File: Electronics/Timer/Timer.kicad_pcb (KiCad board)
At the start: 2 copper layers, 13 parts, among them J1 RJ12-UNSHLD, U1 74HC165

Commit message: Updated trace routing on timer circuit
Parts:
- moved C1 29.8 mm to (75.5, 66.0)
- moved C2 29.8 mm to (44.2, 41.2)
- moved D1 29.8 mm to (64.2, 41.2)
- moved D2 29.8 mm to (71.5, 51.0)
- moved J1 29.8 mm to (61.2, 21.2)
- moved R1 29.8 mm to (74.5, 47.2)
- moved RN1 29.8 mm to (53.8, 65.8)
- moved S1 29.8 mm to (33.0, 82.0)
- moved S2 29.8 mm to (46.5, 80.2)
- moved S3 29.8 mm to (59.2, 80.5)
- moved S4 29.8 mm to (71.2, 80.5)
- moved S5 29.8 mm to (96.5, 81.5)
- moved U1 29.8 mm to (69.0, 54.0)
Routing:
- net Net-(RN1-Pad6): track 34.0 -> 79.9 mm, vias 0 -> 2
- net /LOAD: track 0.00 -> 36.2 mm, vias 0 -> 2
- net GND: track 182.5 -> 186.4 mm
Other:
- board outline added: 86.2 x 73.5 mm

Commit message: Updated Timer schematic and updated PCB footprints
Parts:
- added C3: 270pF, Capacitors_SMD:C_0603_HandSoldering, B.Cu at (49.8, 44.2)
- added D3: D_Zener, Diodes_SMD:SOD-80C, B.Cu at (49.5, 48.3)
- added D4: D_Zener, Diodes_SMD:SOD-80C, B.Cu at (70.9, 29.2)
- added R2: 10, Resistors_SMD:R_1206_HandSoldering, B.Cu at (59.2, 44.7)
- added R3: 470, Resistors_SMD:R_1206_HandSoldering, B.Cu at (43.9, 46.2)
- added R4: 470, Resistors_SMD:R_1206_HandSoldering, B.Cu at (59.4, 32.8)
- C1: value C -> 270pF; footprint Capacitors_THT:C_Disc_D4.3mm_W1.9mm_P5.00mm -> Capacitors_SMD:C_0603_HandSoldering; moved to B.Cu
- C2: value CP1 -> 10uF; footprint Capacitors_THT:CP_Axial_L10.0mm_D6.0mm_P15.00mm_Horizontal -> Capacitors_SMD:C_1210_HandSoldering; moved to B.Cu
- D2: value D -> D_Zener; footprint Diodes_THT:D_A-405_P5.08mm_Vertical_AnodeUp -> Diodes_SMD:SOD-80C; moved to B.Cu
- R1: value R -> 68; footprint Resistors_THT:R_Axial_DIN0309_L9.0mm_D3.2mm_P2.54mm_Vertical -> Resistors_SMD:R_1206_HandSoldering; moved to B.Cu
- moved C1 19.3 mm to (62.5, 51.8)
- moved C2 14.0 mm to (56.4, 48.3), turned to 180 degrees
- moved D2 8.22 mm to (63.8, 48.3)
- moved R1 7.47 mm to (67.3, 45.2), turned to 0 degrees
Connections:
- D2 pad 2: /CLK -> GND
- J1 pad 2: /CLK -> Net-(J1-Pad2)
- J1 pad 3: /LOAD -> Net-(J1-Pad3)
- J1 pad 4: Net-(J1-Pad4) -> Net-(C3-Pad1)
- R1 pad 1: +3V3 -> Net-(J1-Pad2)
- U1 pad 2: /CLK -> +3V3
- U1 pad 9: Net-(J1-Pad4) -> Net-(D3-Pad1)
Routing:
- net Net-(J1-Pad4): track 70.6 -> 0.00 mm
- net Net-(C3-Pad1): track 0.00 -> 62.6 mm
- net GND: track 186.4 -> 234.8 mm
- net /CLK: track 28.3 -> 0.00 mm
- net Net-(J1-Pad2): track 0.00 -> 25.2 mm
- net Net-(D3-Pad1): track 0.00 -> 20.4 mm
- net +3V3: track 223.2 -> 203.0 mm
- net Net-(J1-Pad3): track 0.00 -> 7.80 mm
- net /LOAD: track 36.2 -> 40.1 mm, vias 2 -> 0
- net Net-(D1-Pad2): track 3.50 -> 6.74 mm

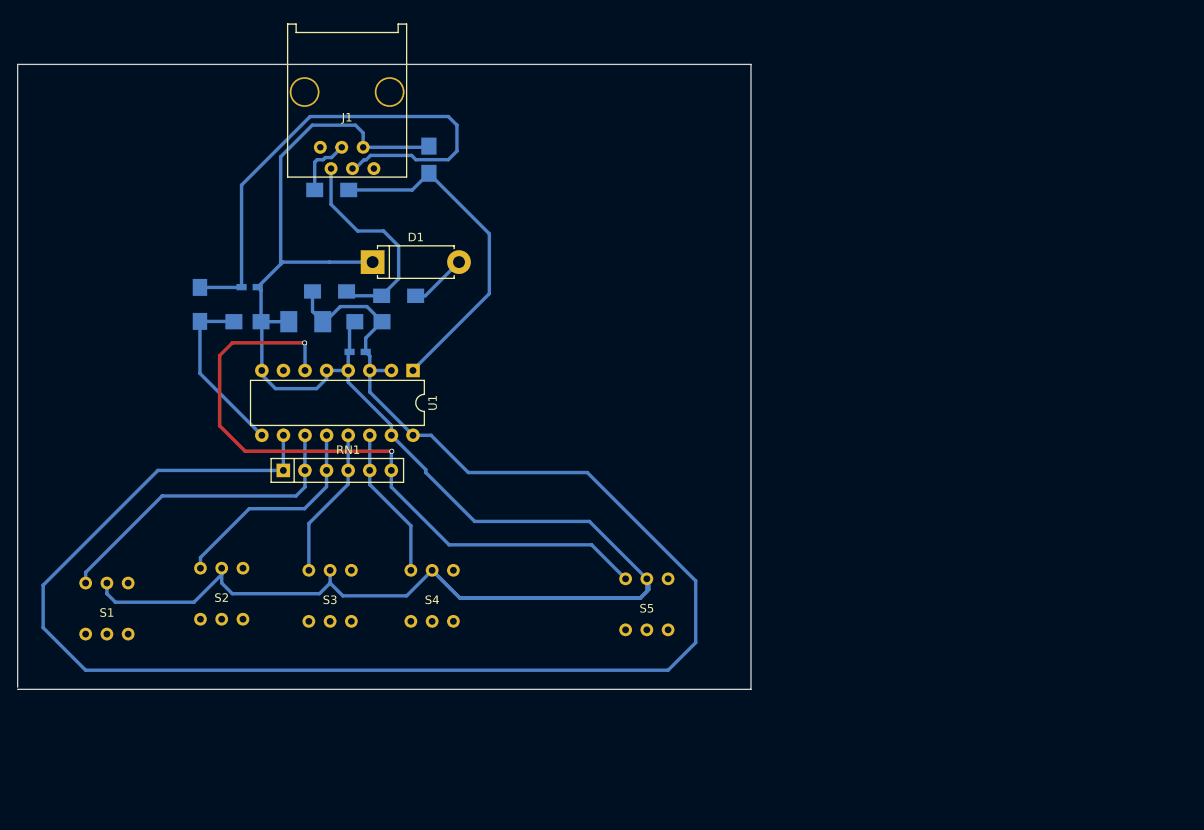
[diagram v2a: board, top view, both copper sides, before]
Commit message: Updated Timer PCB and exported GERBERS
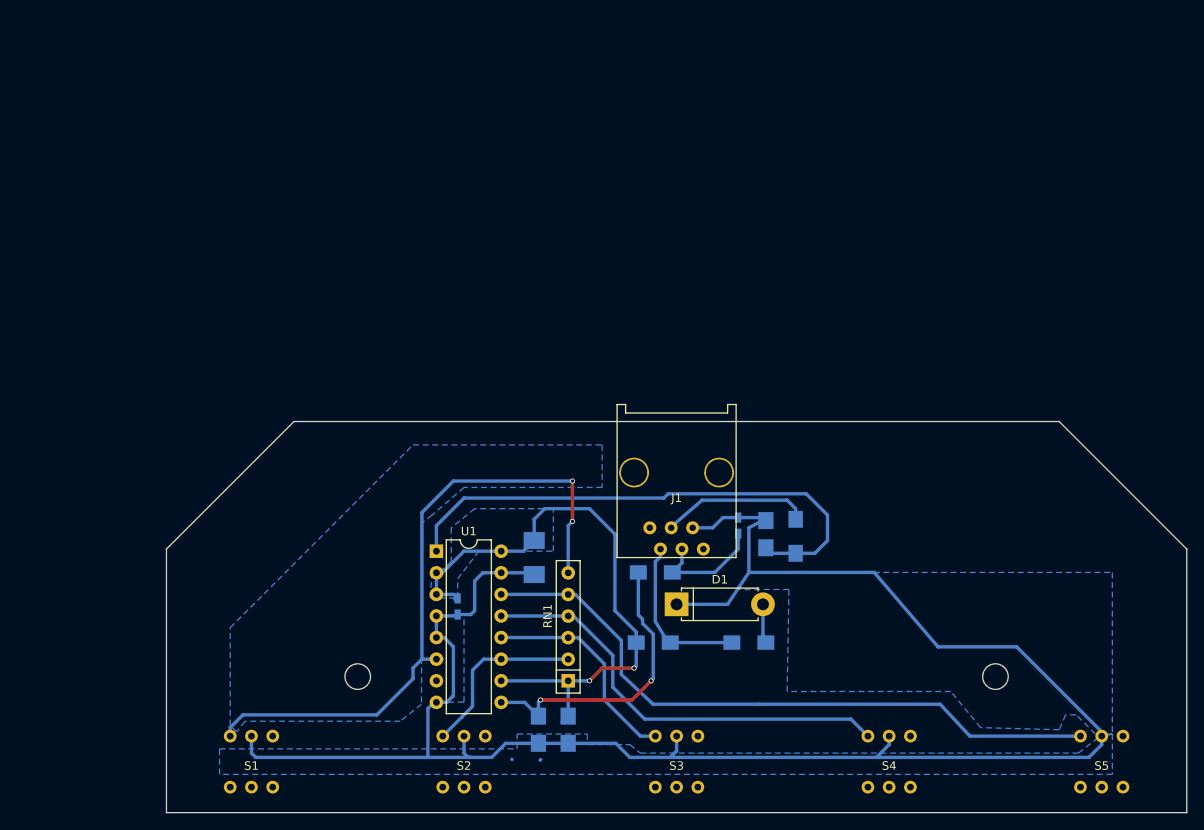
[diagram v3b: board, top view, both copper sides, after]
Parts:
- moved R4 68.1 mm to (114.0, 73.5), turned to 270 degrees
- moved C3 63.9 mm to (107.2, 72.2), turned to 90 degrees
- moved R3 62.1 mm to (97.5, 77.8), turned to 180 degrees
- moved D4 59.2 mm to (110.5, 73.2)
- moved J1 59.2 mm to (100.0, 66.0)
- moved D3 58.9 mm to (83.8, 96.2), turned to 270 degrees
- moved R1 58.0 mm to (108.5, 86.0)
- moved S4 57.2 mm to (125.0, 100.0)
- moved S5 56.6 mm to (150.0, 100.0)
- moved R2 56.2 mm to (97.2, 86.0)
- moved D1 53.8 mm to (100.0, 81.5)
- moved D2 53.4 mm to (87.2, 96.2), turned to 270 degrees
- moved S3 45.2 mm to (100.0, 100.0)
- moved RN1 41.7 mm to (87.2, 90.5), turned to 90 degrees
- moved C2 38.6 mm to (83.2, 76.0), turned to 270 degrees
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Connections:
- S1 pad 1: Net-(RN1-Pad2) -> Net-(RN1-Pad6)
- S2 pad 1: Net-(RN1-Pad3) -> Net-(RN1-Pad2)
- S3 pad 1: Net-(RN1-Pad4) -> Net-(RN1-Pad3)
- S4 pad 1: Net-(RN1-Pad5) -> Net-(RN1-Pad4)
- S5 pad 1: Net-(RN1-Pad6) -> Net-(RN1-Pad5)
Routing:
- net +3V3: track 203.0 -> 71.2 mm, vias 0 -> 2
- net Net-(RN1-Pad5): track 17.9 -> 77.4 mm
- net Net-(C3-Pad1): track 62.6 -> 13.9 mm
- net Net-(RN1-Pad4): track 17.8 -> 51.2 mm
- net /LOAD: track 40.1 -> 62.8 mm
- net Net-(RN1-Pad2): track 37.3 -> 21.0 mm
- net Net-(D3-Pad1): track 20.4 -> 34.6 mm, vias 0 -> 2
- net Net-(J1-Pad3): track 7.80 -> 17.6 mm
- net GND: track 234.8 -> 228.7 mm
- net Net-(J1-Pad2): track 25.2 -> 19.2 mm
- net Net-(D1-Pad2): track 6.74 -> 3.79 mm
- net Net-(RN1-Pad6): track 79.9 -> 77.5 mm
- added copper zone on B.Cu, net +3V3
- added copper zone on B.Cu, net GND
- added copper zone on B.Cu, net Net-(RN1-Pad6)
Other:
- board size 86.2 x 73.5 mm -> 120 x 46 mm
- net class 1mm added: clearance 0.3, trace_width 1, via_dia 0.6, via_drill 0.4

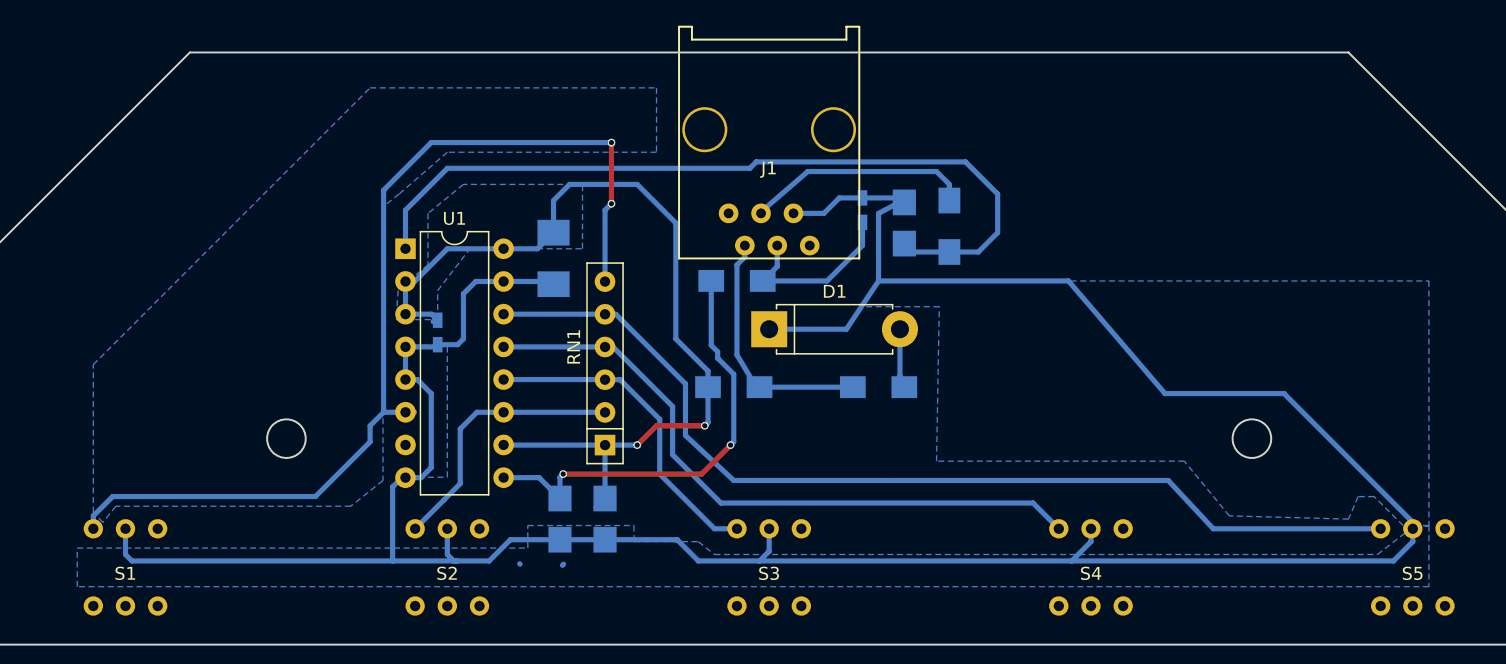
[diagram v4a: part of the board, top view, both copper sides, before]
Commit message: Timer: Restore David's updated schematic and PCB from earlier failed merge.
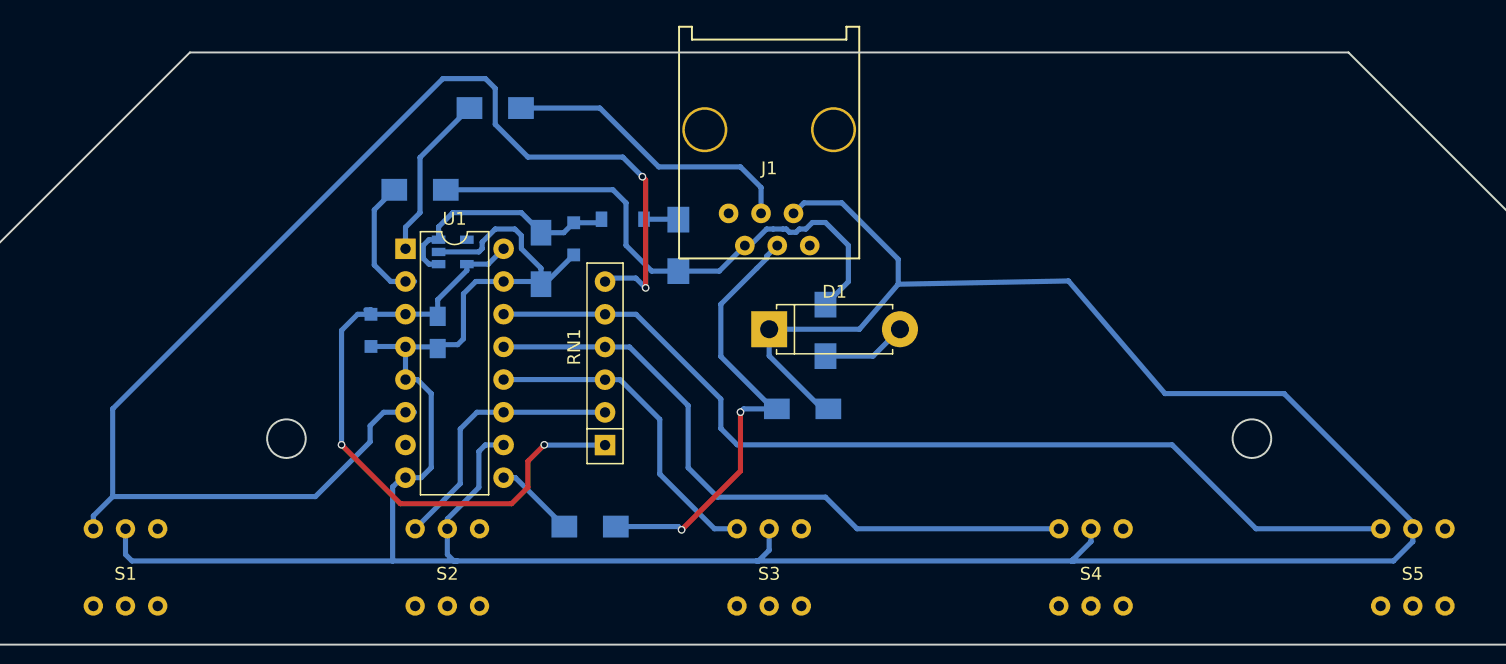
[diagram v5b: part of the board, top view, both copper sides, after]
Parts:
- added R5: 470, Resistors_SMD:R_1206_HandSoldering, B.Cu at (72.9, 70.7)
- added U2: MIC5504-3.3YM5, TO_SOT_Packages_SMD:SOT-23-5, B.Cu at (75.4, 75.5)
- C1: value 270pF -> 10nF; footprint Capacitors_SMD:C_0603_HandSoldering -> Capacitors_SMD:C_0805_HandSoldering
- C2: value 10uF -> 1uF; footprint Capacitors_SMD:C_1210_HandSoldering -> Capacitors_SMD:C_1206_HandSoldering
- C3: value 270pF -> 470pF; footprint Capacitors_SMD:C_0603_HandSoldering -> Capacitors_SMD:C_1206_HandSoldering
- D2: value D_Zener -> D_Zener_5V; footprint Diodes_SMD:SOD-80C -> Diodes_SMD:D_SOD-323_HandSoldering
- D3: value D_Zener -> D_Schottky; footprint Diodes_SMD:SOD-80C -> Diodes_SMD:D_SOD-123
- D4: value D_Zener -> D_Zener_3.3V; footprint Diodes_SMD:SOD-80C -> Diodes_SMD:D_SOD-323_HandSoldering
- R1: value 68 -> 470
- R2: value 10 -> 100
- R3: value 470 -> 10
- moved D4 42.3 mm to (69.1, 81.6), turned to 270 degrees
- moved R4 36.5 mm to (78.7, 64.3), turned to 180 degrees
- moved D3 23.8 mm to (88.6, 73.0), turned to 0 degrees
- moved R3 22.2 mm to (86.1, 96.8)
- moved D2 21.9 mm to (84.8, 74.5)
- moved C3 16.1 mm to (102.6, 87.7), turned to 0 degrees
- moved R2 11.8 mm to (92.9, 75.0), turned to 90 degrees
- moved R1 6.04 mm to (104.4, 81.6), turned to 90 degrees
- moved C2 0.97 mm to (82.3, 76.0)
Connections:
- net Net-(C3-Pad1) renamed /Q-Out
- C2 pad 1: +3V3 -> /5V-In
- D2 pad 1: +3V3 -> /5V-In
- D3 pad 1: Net-(D3-Pad1) -> /5V-In
- D3 pad 2: GND -> Net-(D3-Pad2)
- D4 pad 1: /LOAD -> +3V3
- J1 pad 2: Net-(J1-Pad2) -> /PWR-CLK-IN
- R1 pad 1: Net-(J1-Pad2) -> Net-(D1-Pad2)
- R1 pad 2: Net-(D1-Pad2) -> /PWR-CLK-IN
- R2 pad 1: Net-(J1-Pad2) -> /PWR-CLK-IN
- R2 pad 2: +3V3 -> Net-(D3-Pad2)
- R3 pad 2: Net-(D3-Pad1) -> /Q
- U1 pad 10: +3V3 -> GND
- U1 pad 2: +3V3 -> /CLK
- U1 pad 9: Net-(D3-Pad1) -> /Q
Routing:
- net /LOAD: track 62.8 -> 13.1 mm
- net /PWR-CLK-IN: track 0.00 -> 43.7 mm
- net Net-(D3-Pad1): track 34.6 -> 0.00 mm, vias 2 -> 0
- net GND: track 228.7 -> 257.9 mm
- net Net-(RN1-Pad6): track 77.5 -> 105.7 mm
- net /Q-Out: track 13.9 -> 35.8 mm, vias 0 -> 2
- net Net-(J1-Pad2): track 19.2 -> 0.00 mm
- net +3V3: track 71.2 -> 52.2 mm
- net /5V-In: track 0.00 -> 19.0 mm
- net /CLK: track 0.00 -> 10.2 mm
- net /Q: track 0.00 -> 6.29 mm
- net Net-(J1-Pad3): track 17.6 -> 23.3 mm
- net Net-(D1-Pad2): track 3.79 -> 6.65 mm
- net Net-(D3-Pad2): track 0.00 -> 2.68 mm
- net Net-(RN1-Pad4): track 51.2 -> 52.4 mm
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- removed copper zone on B.Cu, net +3V3
- removed copper zone on B.Cu, net GND
- removed copper zone on B.Cu, net Net-(RN1-Pad6)

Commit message: Revert "Merge branch 'master' into electronics-tweaks; overwrite 'master' hat changes"
This reverts commit 8490e2c3782f3b2eaf596155d8884dc6cd65858c, reversing
changes made to 143268d8e254d2edd056497eb53e137ee58f0f7c.
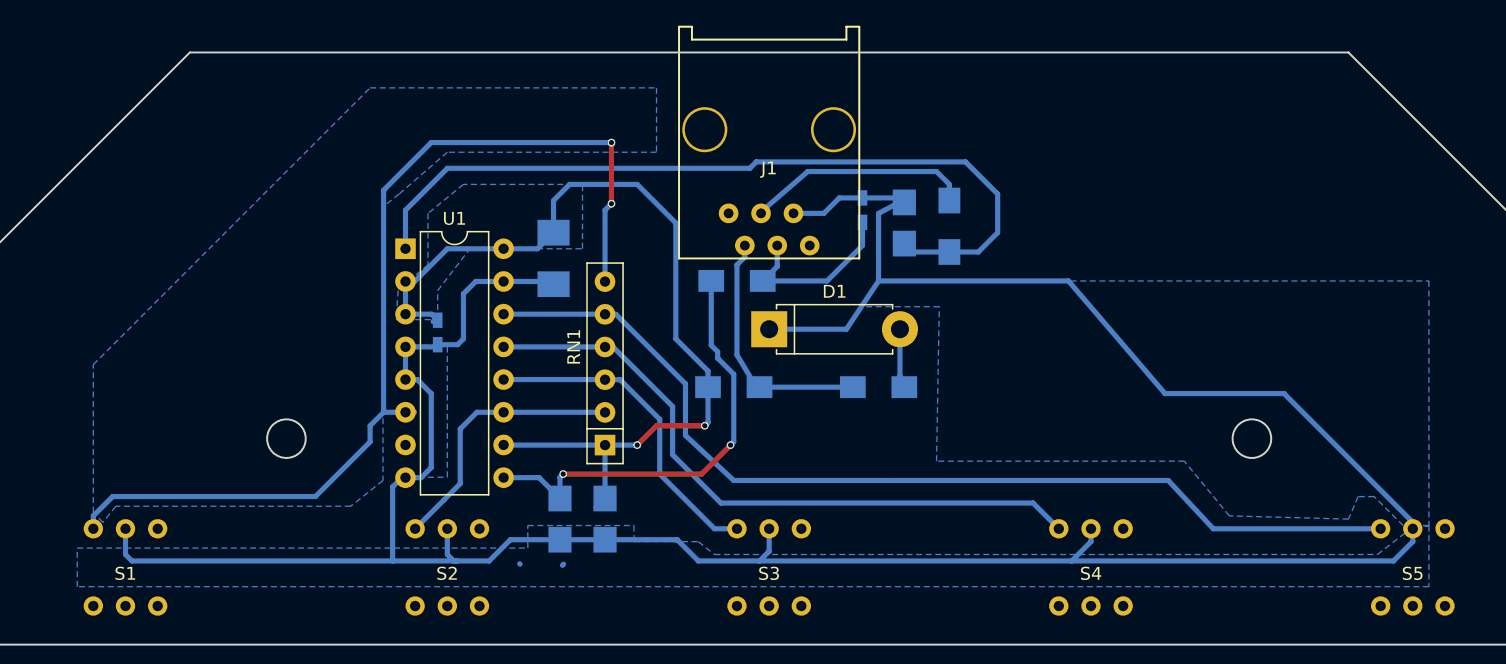
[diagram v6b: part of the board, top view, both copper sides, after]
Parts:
- removed R5: 470, Resistors_SMD:R_1206_HandSoldering
- removed U2: MIC5504-3.3YM5, TO_SOT_Packages_SMD:SOT-23-5
- C1: value 10nF -> 270pF; footprint Capacitors_SMD:C_0805_HandSoldering -> Capacitors_SMD:C_0603_HandSoldering
- C2: value 1uF -> 10uF; footprint Capacitors_SMD:C_1206_HandSoldering -> Capacitors_SMD:C_1210_HandSoldering
- C3: value 470pF -> 270pF; footprint Capacitors_SMD:C_1206_HandSoldering -> Capacitors_SMD:C_0603_HandSoldering
- D2: value D_Zener_5V -> D_Zener; footprint Diodes_SMD:D_SOD-323_HandSoldering -> Diodes_SMD:SOD-80C
- D3: value D_Schottky -> D_Zener; footprint Diodes_SMD:D_SOD-123 -> Diodes_SMD:SOD-80C
- D4: value D_Zener_3.3V -> D_Zener; footprint Diodes_SMD:D_SOD-323_HandSoldering -> Diodes_SMD:SOD-80C
- R1: value 470 -> 68
- R2: value 100 -> 10
- R3: value 10 -> 470
- moved D4 42.3 mm to (110.5, 73.2), turned to 90 degrees
- moved R4 36.5 mm to (114.0, 73.5), turned to 270 degrees
- moved D3 23.8 mm to (83.8, 96.2), turned to 270 degrees
- moved R3 22.2 mm to (97.5, 77.8)
- moved D2 21.9 mm to (87.2, 96.2)
- moved C3 16.1 mm to (107.2, 72.2), turned to 90 degrees
- moved R2 11.8 mm to (97.2, 86.0), turned to 180 degrees
- moved R1 6.04 mm to (108.5, 86.0), turned to 0 degrees
- moved C2 0.97 mm to (83.2, 76.0)
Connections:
- net /Q-Out renamed Net-(C3-Pad1)
- C2 pad 1: /5V-In -> +3V3
- D2 pad 1: /5V-In -> +3V3
- D3 pad 1: /5V-In -> Net-(D3-Pad1)
- D3 pad 2: Net-(D3-Pad2) -> GND
- D4 pad 1: +3V3 -> /LOAD
- J1 pad 2: /PWR-CLK-IN -> Net-(J1-Pad2)
- R1 pad 1: Net-(D1-Pad2) -> Net-(J1-Pad2)
- R1 pad 2: /PWR-CLK-IN -> Net-(D1-Pad2)
- R2 pad 1: /PWR-CLK-IN -> Net-(J1-Pad2)
- R2 pad 2: Net-(D3-Pad2) -> +3V3
- R3 pad 2: /Q -> Net-(D3-Pad1)
- U1 pad 10: GND -> +3V3
- U1 pad 2: /CLK -> +3V3
- U1 pad 9: /Q -> Net-(D3-Pad1)
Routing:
- net /LOAD: track 13.1 -> 62.8 mm
- net /PWR-CLK-IN: track 43.7 -> 0.00 mm
- net Net-(D3-Pad1): track 0.00 -> 34.6 mm, vias 0 -> 2
- net GND: track 257.9 -> 228.7 mm
- net Net-(RN1-Pad6): track 105.7 -> 77.5 mm
- net Net-(C3-Pad1): track 35.8 -> 13.9 mm, vias 2 -> 0
- net Net-(J1-Pad2): track 0.00 -> 19.2 mm
- net +3V3: track 52.2 -> 71.2 mm
- net /5V-In: track 19.0 -> 0.00 mm
- net /CLK: track 10.2 -> 0.00 mm
- net /Q: track 6.29 -> 0.00 mm
- net Net-(J1-Pad3): track 23.3 -> 17.6 mm
- net Net-(D1-Pad2): track 6.65 -> 3.79 mm
- net Net-(D3-Pad2): track 2.68 -> 0.00 mm
- net Net-(RN1-Pad4): track 52.4 -> 51.2 mm
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- added copper zone on B.Cu, net +3V3
- added copper zone on B.Cu, net GND
- added copper zone on B.Cu, net Net-(RN1-Pad6)
